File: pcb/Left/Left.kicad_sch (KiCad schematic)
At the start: 0 parts

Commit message: updateee
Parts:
- added B_LED1: LED_0603_Blue, PCM_LED_SMD_AKL:LED_0603_1608Metric, symbol PCM_LED_AKL:LED_0603_Blue
- added C1, C10, C11, C12, C13, C14, C15, C16, C17, C18, C19, C2, C20, C21, C22, C23, C24, C25, C26, C27, C28, C29, C3, C30, C31, C32, C33, C34, C35, C36, C37, C38, C39, C4, C40, C41, C42, C43, C44, C45, C46, C47, C48, C5, C6, C7, C8, C9, ShifterC1, USBI_C1, USB_C1: 0.1uF, Capacitor_SMD:C_0805_2012Metric_Pad1.18x1.45mm_HandSolder, symbol Device:C
- added C49, C50: 1u, Capacitor_SMD:C_0805_2012Metric_Pad1.18x1.45mm_HandSolder, symbol Device:C_Small
- added C51, C52, C53: 4.7uF, Capacitor_SMD:C_0805_2012Metric_Pad1.18x1.45mm_HandSolder, symbol Device:C
- added C54: 0.1u, Capacitor_SMD:C_0805_2012Metric_Pad1.18x1.45mm_HandSolder, symbol Device:C
- added D1, D10, D11, D12, D13, D14, D15, D16, D17, D18, D19, D2, D20, D21, D22, D23, D24, D25, D26, D27, D28, D29, D3, D30, D31, D32, D33, D34, D35, D36, D37, D38, D39, D4, D40, D41, D42, D43, D44, D45, D46, D47, D48, D5, D6, D7, D8, D9: D, SplitKeeb:D_SOD-123, symbol Device:D
- added ESD_D1, ESD_D2: USBLC6-2SC6, PCM_Package_TO_SOT_SMD_AKL:SOT-23-6, symbol PCM_Diode_TVS_AKL:USBLC6-2SC6
- added F1: 750mA, Fuse:Fuse_1206_3216Metric_Pad1.42x1.75mm_HandSolder, symbol Device:Polyfuse
- added G_LED1: LED_0603_Green, PCM_LED_SMD_AKL:LED_0603_1608Metric, symbol PCM_LED_AKL:LED_0603_Green
- added H1, H2, H3, H4, H5, H6: MountingHole, MountingHole:MountingHole_3.2mm_M3_Pad_TopBottom, symbol Mechanical:MountingHole
- added J1, J4: USB_C_Receptacle_USB2.0_16P, PCM_marbastlib-various:USB_C_Receptacle_HRO_TYPE-C-31-M-23, symbol Connector:USB_C_Receptacle_USB2.0_16P
- added J3: JST_2mm_LiPo, PCM_SparkFun-Connector:JST_1x02_P2.0mm_Horizontal_SMD, symbol PCM_SparkFun-Connector:Conn_01x02_JST_P2.0mm_Horizontal_SMD_LiPo
- added J5: DEV_HEADERS, PCM_fab:PinHeader_01x05_P2.54mm_Vertical_THT_D1mm, symbol PCM_fab:PinHeader_01x05_P2.54mm_Vertical_THT_D1mm
- added JP1, JP2: SolderJumper, Jumper:SolderJumper-3_P1.3mm_Open_RoundedPad1.0x1.5mm_NumberLabels, symbol Jumper:SolderJumper_3_Open
- added LED1, LED10, LED11, LED12, LED13, LED14, LED15, LED16, LED17, LED18, LED19, LED2, LED20, LED21, LED22, LED23, LED24, LED25, LED26, LED27, LED28, LED29, LED3, LED30, LED31, LED32, LED33, LED34, LED35, LED36, LED37, LED38, LED39, LED4, LED40, LED41, LED42, LED43, LED44, LED45, LED46, LED47, LED48, LED5, LED6, LED7, LED8, LED9: MX_SK6812MINI-E, PCM_marbastlib-mx:LED_MX_6028R-ROT, symbol PCM_marbastlib-mx:MX_SK6812MINI-E
- added OLED1: nice!view, nice_view:nice_view, symbol nice_view:nice!view
- added PC1, PC2: 0.1u, Capacitor_SMD:C_0805_2012Metric_Pad1.18x1.45mm_HandSolder, symbol Device:C_Small
- added Q1: 2N7002, PCM_Package_TO_SOT_SMD_AKL:SOT-23, symbol PCM_Transistor_MOSFET_AKL:2N7002
- added R1, R2, R5, R9: 10k, Resistor_SMD:R_0805_2012Metric_Pad1.20x1.40mm_HandSolder, symbol Device:R
- added R10: 806/820k, Resistor_SMD:R_0805_2012Metric_Pad1.20x1.40mm_HandSolder, symbol Device:R
- added R11: 2M, Resistor_SMD:R_0805_2012Metric_Pad1.20x1.40mm_HandSolder, symbol Device:R
- added R12: 470, Resistor_SMD:R_0805_2012Metric_Pad1.20x1.40mm_HandSolder, symbol Device:R
- added R13, R14, USBR1, USBR2: 5.1k, Resistor_SMD:R_0805_2012Metric_Pad1.20x1.40mm_HandSolder, symbol Device:R
- added R15, R17: 1k, Resistor_SMD:R_0805_2012Metric_Pad1.20x1.40mm_HandSolder, symbol Device:R
- added R3: 100k, Resistor_SMD:R_0805_2012Metric_Pad1.20x1.40mm_HandSolder, symbol Device:R
- added R4: 100R, Resistor_SMD:R_0805_2012Metric_Pad1.20x1.40mm_HandSolder, symbol Device:R
- added R6: 47k, Resistor_SMD:R_0805_2012Metric_Pad1.20x1.40mm_HandSolder, symbol Device:R
- added R7: 1.5k, Resistor_SMD:R_0805_2012Metric_Pad1.20x1.40mm_HandSolder, symbol Device:R
- added R8: 3.9k, Resistor_SMD:R_0805_2012Metric_Pad1.20x1.40mm_HandSolder, symbol Device:R
- added Reset_Btn1: SW_Push, Button_Switch_SMD:Panasonic_EVQPUL_EVQPUC, symbol Switch:SW_Push
- added SW1, SW10, SW11, SW12, SW13, SW14, SW15, SW16, SW18, SW19, SW2, SW20, SW21, SW22, SW23, SW24, SW26, SW27, SW28, SW29, SW3, SW30, SW31, SW32, SW34, SW35, SW36, SW37, SW38, SW39, SW4, SW40, SW43, SW44, SW45, SW5, SW6, SW7, SW8, SW9: SW_Push, PCM_marbastlib-xp-mx:SW_MX_HS_KS-2P02B01-01_1u, symbol Switch:SW_Push_45deg
- added SW17, SW46: SW_Push, PCM_marbastlib-xp-mx:SW_MX_HS_KS-2P02B01-01_1.25u, symbol Switch:SW_Push_45deg
- added SW25, SW41, SW42, SW47: SW_Push, PCM_marbastlib-xp-mx:SW_MX_HS_KS-2P02B01-01_1.5u, symbol Switch:SW_Push_45deg
- added SW33, SW48: SW_Push, PCM_marbastlib-xp-mx:SW_MX_HS_KS-2P02B01-01_1.75u, symbol Switch:SW_Push_45deg
- added SW49: SW_PWR, PCM_marbastlib-various:SW_MSK12C02-HB, symbol Switch:SW_SPDT
- added U1: XC6206PxxxMR, Package_TO_SOT_SMD:SOT-23-3, symbol Regulator_Linear:XC6206PxxxMR
- added U2: BQ24075RGT, Package_DFN_QFN:VQFN-16-1EP_3x3mm_P0.5mm_EP1.6x1.6mm, symbol Battery_Management:BQ24075RGT
- added U3: nRF52840_holyiot_18010, PCM_marbastlib-various:nRF52840_holyiot_18010, symbol PCM_marbastlib-various:nRF52840_holyiot_18010
- added U4: SN74LV1T125DBV, Package_TO_SOT_SMD:SOT-23-5, symbol Logic_LevelTranslator:SN74LV1T125DBV
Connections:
- new net: D23.2 (A), SW23.2
- new net: LED43.2 (DOUT), LED44.3 (DIN)
- new net: LED42.2 (DOUT), LED43.3 (DIN)
- new net: D47.2 (A), SW47.2
- new net: D42.2 (A), SW42.2
- new net: R3.1, SW49.1 (A)
- new net: LED28.2 (DOUT), LED29.3 (DIN)
- new net: LED27.2 (DOUT), LED28.3 (DIN)
- new net: D27.2 (A), SW27.2
- new net: Q1.1 (G), R4.1, R5.2
- new net: ESD_D1.1 (L1), J1.A7 (D-), J1.B7 (D-)
- new net: ESD_D1.3 (L2), J1.A6 (D+), J1.B6 (D+)
- new net: LED45.2 (DOUT), LED46.3 (DIN)
- new net: LED44.2 (DOUT), LED45.3 (DIN)
- new net: D10.2 (A), SW10.2
- new net: LED4.3 (DIN), LED5.2 (DOUT)
- new net: LED5.3 (DIN), LED6.2 (DOUT)
- new net: D26.2 (A), SW26.2
- new net: LED3.3 (DIN), LED4.2 (DOUT)
- new net: D45.2 (A), SW45.2
- new net: LED34.3 (DIN), LED35.2 (DOUT)
- new net: LED35.3 (DIN), LED36.2 (DOUT)
- new net: D19.2 (A), SW19.2
- new net: LED10.3 (DIN), LED9.2 (DOUT)
- new net: LED1.2 (DOUT), LED9.3 (DIN)
- new net: LED21.3 (DIN), LED22.2 (DOUT)
- new net: LED22.3 (DIN), LED23.2 (DOUT)
- new net: LED23.3 (DIN), LED24.2 (DOUT)
- new net: LED16.2 (DOUT), LED24.3 (DIN)
- new net: D14.2 (A), SW14.2
- new net: ESD_D2.1 (L1), J4.A7 (D-), J4.B7 (D-)
- new net: ESD_D2.3 (L2), J4.A6 (D+), J4.B6 (D+)
- new net: LED6.3 (DIN), LED7.2 (DOUT)
- new net: LED7.3 (DIN), LED8.2 (DOUT)
- new net: D33.2 (A), SW33.2
- new net: D29.2 (A), SW29.2
- new net: R12.2, U4.4 (Y)
- new net: D41.2 (A), SW41.2
- new net: D39.2 (A), SW39.2
- new net: D3.2 (A), SW3.2
- new net: D11.2 (A), SW11.2
- new net: D38.2 (A), SW38.2
- new net: D12.2 (A), SW12.2
- new net: D2.2 (A), SW2.2
- new net: F1.1, J4.A4 (VBUS), J4.A9 (VBUS), J4.B4 (VBUS), J4.B9 (VBUS)
- new net: J4.A5 (CC1), R13.1
- new net: J4.B5 (CC2), R14.1
- new net: LED2.3 (DIN), LED3.2 (DOUT)
- new net: LED11.2 (DOUT), LED12.3 (DIN)
- new net: LED10.2 (DOUT), LED11.3 (DIN)
- new net: D30.2 (A), SW30.2
- new net: LED36.3 (DIN), LED37.2 (DOUT)
- new net: D8.2 (A), SW8.2
- new net: D5.2 (A), SW5.2
- new net: D22.2 (A), SW22.2
- new net: D21.2 (A), SW21.2
- new net: LED13.2 (DOUT), LED14.3 (DIN)
- new net: LED12.2 (DOUT), LED13.3 (DIN)
- new net: LED47.2 (DOUT), LED48.3 (DIN)
- new net: LED46.2 (DOUT), LED47.3 (DIN)
- new net: LED33.3 (DIN), LED34.2 (DOUT)
- new net: D37.2 (A), SW37.2
- new net: LED37.3 (DIN), LED38.2 (DOUT)
- new net: LED38.3 (DIN), LED39.2 (DOUT)
- new net: D20.2 (A), SW20.2
- new net: LED20.3 (DIN), LED21.2 (DOUT)
- new net: LED15.2 (DOUT), LED16.3 (DIN)
- new net: LED14.2 (DOUT), LED15.3 (DIN)
- new net: LED31.2 (DOUT), LED32.3 (DIN)
- new net: LED30.2 (DOUT), LED31.3 (DIN)
- new net: LED19.3 (DIN), LED20.2 (DOUT)
- new net: D7.2 (A), SW7.2
- new net: J1.B5 (CC2), USBR2.1
- new net: LED1.3 (DIN), LED2.2 (DOUT)
- new net: D46.2 (A), SW46.2
- new net: D15.2 (A), SW15.2
- new net: D6.2 (A), SW6.2
- new net: R9.2, U2.1 (TS)
- new net: G_LED1.2 (A), R17.2
- new net: D35.2 (A), SW35.2
- new net: D9.2 (A), SW9.2
- new net: LED32.2 (DOUT), LED40.3 (DIN)
- new net: D25.2 (A), SW25.2
- new net: D17.2 (A), SW17.2
- new net: D16.2 (A), SW16.2
- new net: D31.2 (A), SW31.2
- new net: D28.2 (A), SW28.2
- new net: LED41.2 (DOUT), LED42.3 (DIN)
- new net: D44.2 (A), SW44.2
- new net: R8.2, U2.16 (ISET)
- new net: J1.A5 (CC1), USBR1.1
- new net: LED29.2 (DOUT), LED30.3 (DIN)
- new net: R6.2, U2.14 (TMR)
- new net: D18.2 (A), SW18.2
- new net: R7.2, U2.12 (ILIM)
- new net: D43.2 (A), SW43.2
- new net: D4.2 (A), SW4.2
- new net: LED25.2 (DOUT), LED26.3 (DIN)
- new net: LED17.2 (DOUT), LED25.3 (DIN)
- new net: D13.2 (A), SW13.2
- new net: D32.2 (A), SW32.2
- new net: D48.2 (A), SW48.2
- new net: D1.2 (A), SW1.2
- new net: LED18.3 (DIN), LED19.2 (DOUT)
- new net: D24.2 (A), SW24.2
- new net: LED39.3 (DIN), LED40.2 (DOUT)
- new net: B_LED1.2 (A), R15.2
- new net: D36.2 (A), SW36.2
- new net: D40.2 (A), SW40.2
- new net: LED17.3 (DIN), LED18.2 (DOUT)
- new net: D34.2 (A), SW34.2
- new net: LED26.2 (DOUT), LED27.3 (DIN)
- new net: LED33.2 (DOUT), LED41.3 (DIN)
- new net +3.3V: C50.1, C54.1, J5.5 (Pin_5), OLED1.3 (VCC), PC1.1, U1.2 (VO), U3.14 (VDD_nRF)
- new net +5V: C1.2, C10.2, C11.2, C12.2, C13.2, C14.2, C15.2, C16.2, C17.2, C18.2, C19.2, C2.2, C20.2, C21.2, C22.2, C23.2, C24.2, C25.2, C26.2, C27.2, C28.2, C29.2, C3.2, C30.2, C31.2, C32.2, C33.2, C34.2, C35.2, C36.2, C37.2, C38.2, C39.2, C4.2, C40.2, C41.2, C42.2, C43.2, C44.2, C45.2, C46.2, C47.2, C48.2, C5.2, C51.1, C6.2, C7.2, C8.2, C9.2, ESD_D1.5 (VP), ESD_D2.5 (VP), F1.2, J1.A4 (VBUS), J1.A9 (VBUS), J1.B4 (VBUS), J1.B9 (VBUS), LED1.1 (VDD), LED10.1 (VDD), LED11.1 (VDD), LED12.1 (VDD), LED13.1 (VDD), LED14.1 (VDD), LED15.1 (VDD), LED16.1 (VDD), LED17.1 (VDD), LED18.1 (VDD), LED19.1 (VDD), LED2.1 (VDD), LED20.1 (VDD), LED21.1 (VDD), LED22.1 (VDD), LED23.1 (VDD), LED24.1 (VDD), LED25.1 (VDD), LED26.1 (VDD), LED27.1 (VDD), LED28.1 (VDD), LED29.1 (VDD), LED3.1 (VDD), LED30.1 (VDD), LED31.1 (VDD), LED32.1 (VDD), LED33.1 (VDD), LED34.1 (VDD), LED35.1 (VDD), LED36.1 (VDD), LED37.1 (VDD), LED38.1 (VDD), LED39.1 (VDD), LED4.1 (VDD), LED40.1 (VDD), LED41.1 (VDD), LED42.1 (VDD), LED43.1 (VDD), LED44.1 (VDD), LED45.1 (VDD), LED46.1 (VDD), LED47.1 (VDD), LED48.1 (VDD), LED5.1 (VDD), LED6.1 (VDD), LED7.1 (VDD), LED8.1 (VDD), LED9.1 (VDD), PC2.1, R4.2, ShifterC1.1, U2.13 (IN), U3.22 (VBUS), U4.5 (VCC), USBI_C1.1, USB_C1.1
- new net +BATT: C53.1, J3.2 (+), R10.1, R3.2, U2.2 (BAT), U2.3 (BAT)
- new net +VSW: C49.1, C52.1, R1.2, R2.2, U1.3 (VI), U2.10 (OUT), U2.11 (OUT), U2.6 (EN1)
- new net BLUE_LED: R15.1, U3.30 (P1.02-LF)
- new net BT_CHG: R1.1, U2.9 (~{CHG}), U3.27 (P1.00)
- new net BT_PGOOD: R2.1, U2.7 (~{PGOOD}), U3.26 (P0.22)
- new net CS: OLED1.5 (CS), U3.19 (P0.21)
- new net D+: ESD_D2.4 (L2), U3.24 (D+)
- new net D-: ESD_D2.6 (L1), U3.23 (D-)
- new net GND: B_LED1.1 (K), C1.1, C10.1, C11.1, C12.1, C13.1, C14.1, C15.1, C16.1, C17.1, C18.1, C19.1, C2.1, C20.1, C21.1, C22.1, C23.1, C24.1, C25.1, C26.1, C27.1, C28.1, C29.1, C3.1, C30.1, C31.1, C32.1, C33.1, C34.1, C35.1, C36.1, C37.1, C38.1, C39.1, C4.1, C40.1, C41.1, C42.1, C43.1, C44.1, C45.1, C46.1, C47.1, C48.1, C49.2, C5.1, C50.2, C51.2, C52.2, C53.2, C54.2, C6.1, C7.1, C8.1, C9.1, ESD_D1.2 (VN), ESD_D2.2 (VN), G_LED1.1 (K), J1.A1 (GND), J1.A12 (GND), J1.B1 (GND), J1.B12 (GND), J1.S1 (SHIELD), J3.1 (-), J4.A1 (GND), J4.A12 (GND), J4.B1 (GND), J4.B12 (GND), J4.S1 (SHIELD), J5.1 (Pin_1), LED1.4 (VSS), LED10.4 (VSS), LED11.4 (VSS), LED12.4 (VSS), LED13.4 (VSS), LED14.4 (VSS), LED15.4 (VSS), LED16.4 (VSS), LED17.4 (VSS), LED18.4 (VSS), LED19.4 (VSS), LED2.4 (VSS), LED20.4 (VSS), LED21.4 (VSS), LED22.4 (VSS), LED23.4 (VSS), LED24.4 (VSS), LED25.4 (VSS), LED26.4 (VSS), LED27.4 (VSS), LED28.4 (VSS), LED29.4 (VSS), LED3.4 (VSS), LED30.4 (VSS), LED31.4 (VSS), LED32.4 (VSS), LED33.4 (VSS), LED34.4 (VSS), LED35.4 (VSS), LED36.4 (VSS), LED37.4 (VSS), LED38.4 (VSS), LED39.4 (VSS), LED4.4 (VSS), LED40.4 (VSS), LED41.4 (VSS), LED42.4 (VSS), LED43.4 (VSS), LED44.4 (VSS), LED45.4 (VSS), LED46.4 (VSS), LED47.4 (VSS), LED48.4 (VSS), LED5.4 (VSS), LED6.4 (VSS), LED7.4 (VSS), LED8.4 (VSS), LED9.4 (VSS), OLED1.4 (GND), PC1.2, PC2.2, Q1.2 (S), R11.2, R13.2, R14.2, R5.1, R6.1, R7.1, R8.1, R9.1, Reset_Btn1.2, SW49.3 (C), ShifterC1.2, U1.1 (GND), U2.17 (VSS), U2.4 (~{CE}), U2.5 (EN2), U2.8 (VSS), U3.1 (GND), U3.25 (GND), U3.37 (GND), U4.1 (~{OE}), U4.3 (GND), USBI_C1.2, USBR1.2, USBR2.2, USB_C1.2
- new net GREEN_LED: R17.1, U3.29 (P1.01-LF)
- new net LINK+: ESD_D1.4 (L2), JP2.2 (C)
- new net LINK-: ESD_D1.6 (L1), JP1.2 (C)
- new net MOSI: OLED1.1 (MOSI), U3.17 (P0.12)
- new net RESET: J5.4 (Pin_4), Reset_Btn1.1, U3.21 (P0.18-RESET)
- new net R_COL1: SW16.1, SW24.1, SW32.1, SW40.1, SW48.1, SW8.1, U3.9 (P0.29-LF-A)
- new net R_COL2: SW15.1, SW23.1, SW31.1, SW39.1, SW47.1, SW7.1, U3.8 (P0.28-LF-A)
- new net R_COL3: SW14.1, SW22.1, SW30.1, SW38.1, SW46.1, SW6.1, U3.7 (P0.02-LF-A)
- new net R_COL4: SW13.1, SW21.1, SW29.1, SW37.1, SW45.1, SW5.1, U3.6 (P0.03-LF-A)
- new net R_COL5: SW12.1, SW20.1, SW28.1, SW36.1, SW4.1, SW44.1, U3.5 (P1.15-LF)
- new net R_COL6: SW11.1, SW19.1, SW27.1, SW3.1, SW35.1, SW43.1, U3.4 (P1.13-LF)
- new net R_COL7: SW10.1, SW18.1, SW2.1, SW26.1, SW34.1, SW42.1, U3.3 (P1.10-LF)
- new net R_COL8: SW1.1, SW17.1, SW25.1, SW33.1, SW41.1, SW9.1, U3.2 (P1.11-LF)
- new net R_LED1: LED8.3 (DIN), R12.1
- new net R_LED_3v3_1: U3.34 (P1.06-LF), U4.2 (A)
- new net R_ROW1: D1.1 (K), D2.1 (K), D3.1 (K), D4.1 (K), D5.1 (K), D6.1 (K), D7.1 (K), D8.1 (K), U3.10 (P0.30-LF-A)
- new net R_ROW2: D10.1 (K), D11.1 (K), D12.1 (K), D13.1 (K), D14.1 (K), D15.1 (K), D16.1 (K), D9.1 (K), U3.11 (P0.31-LF-A)
- new net R_ROW3: D17.1 (K), D18.1 (K), D19.1 (K), D20.1 (K), D21.1 (K), D22.1 (K), D23.1 (K), D24.1 (K), U3.12 (P0.04-A)
- new net R_ROW4: D25.1 (K), D26.1 (K), D27.1 (K), D28.1 (K), D29.1 (K), D30.1 (K), D31.1 (K), D32.1 (K), U3.13 (P0.05-A)
- new net R_ROW5: D33.1 (K), D34.1 (K), D35.1 (K), D36.1 (K), D37.1 (K), D38.1 (K), D39.1 (K), D40.1 (K), U3.15 (P0.07)
- new net R_ROW6: D41.1 (K), D42.1 (K), D43.1 (K), D44.1 (K), D45.1 (K), D46.1 (K), D47.1 (K), D48.1 (K), U3.16 (P1.09)
- new net SCK: OLED1.2 (SCK), U3.18 (P0.23)
- new net SWDCLK: J5.3 (Pin_3), U3.31 (SWDCLK)
- new net SWDIO: J5.2 (Pin_2), U3.32 (SWDIO)
- new net SYS_OFF: Q1.3 (D), SW49.2 (B), U2.15 (SYSOFF)
- new net USART_RX: JP1.1 (A), JP2.1 (A), U3.36 (P0.10-LF-NFC)
- new net USART_TX: JP1.3 (B), JP2.3 (B), U3.35 (P0.09-LF-NFC)
- new net VSENSE: R10.2, R11.1, U3.33 (P1.04-LF)
- no-connect marks 0 -> 25
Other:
- note added: "Battery"
- note added: "Battery Management"
- note added: "Default pins for nice view CS = D1 / P0.06 SCL = D2 / 0.20 MOSI = D3 / P0.17"
- note added: "Display"
- note added: "Interconnector USB C"
- note added: "Logic level shifter"
- note added: "MCU"
- note added: "Mounting Holes"
- note added: "Neopixels"
- note added: "Status LEDs"
- note added: "Switches"
- note added: "USB C"
- note added: "Voltage sensing"

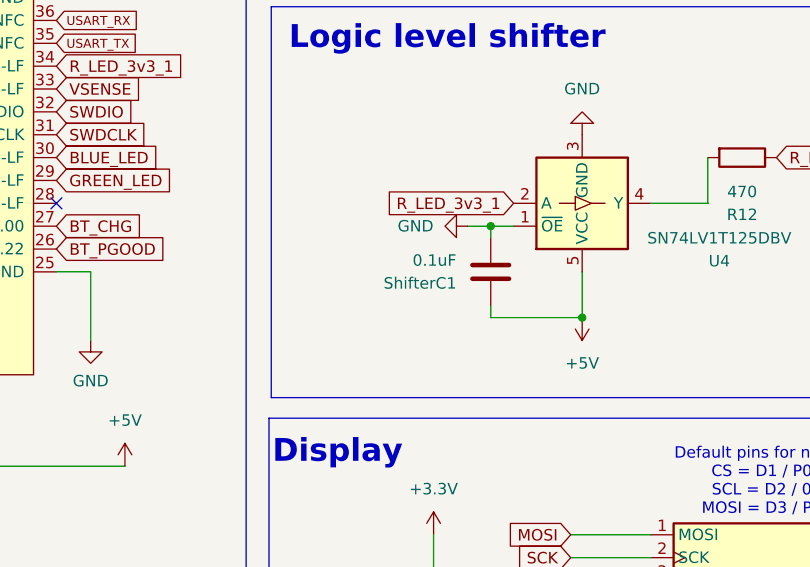
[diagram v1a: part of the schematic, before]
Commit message: update bom add images
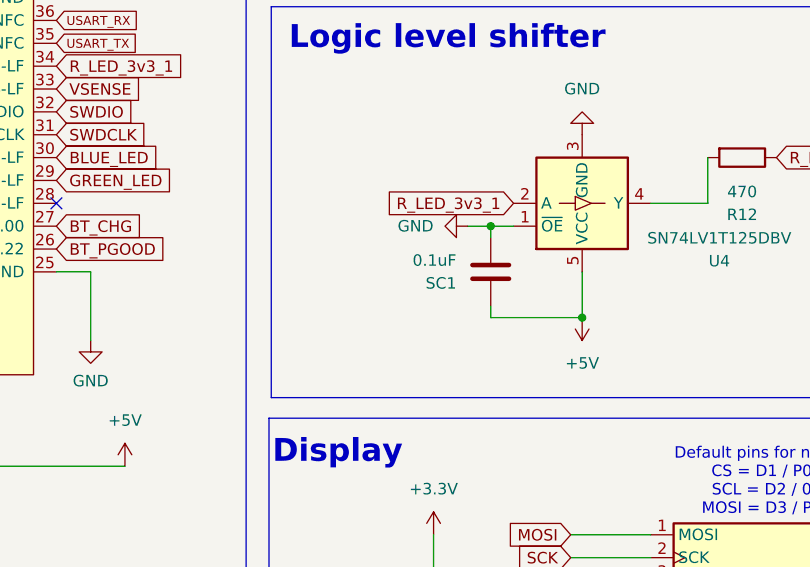
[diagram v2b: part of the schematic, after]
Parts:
- renumbered ShifterC1 to SC1
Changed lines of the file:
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@@
 		(on_board yes)
 		(dnp no)
-		(property "Reference" "ShifterC1"
+		(property "Reference" "SC1"
 			(at 229.87 321.3101 0)
 			(effects
@@
 			(project "Right"
 				(path "/0513b6e3-358c-4d14-8376-31298e27d8df"
-					(reference "ShifterC1")
+					(reference "SC1")
 					(unit 1)
 				)
